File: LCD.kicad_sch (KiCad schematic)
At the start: 1 part, among them U5 LCD_ILI9341

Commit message: sebelum pemeriksaan terkahir
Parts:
- added BZ1: Buzzer, symbol Device:Buzzer
- added C73: 4.7uF, symbol Device:C
- added R47: 100 ohm, symbol Device:R_US
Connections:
- net GND: now also BZ1.2 (-), C73.2
- net ILI9341_VCC renamed DCDC_3V3
- net DCDC_3V3: now also C73.1
- new net: BZ1.1 (+), R47.2
- new net buzzer: R47.1

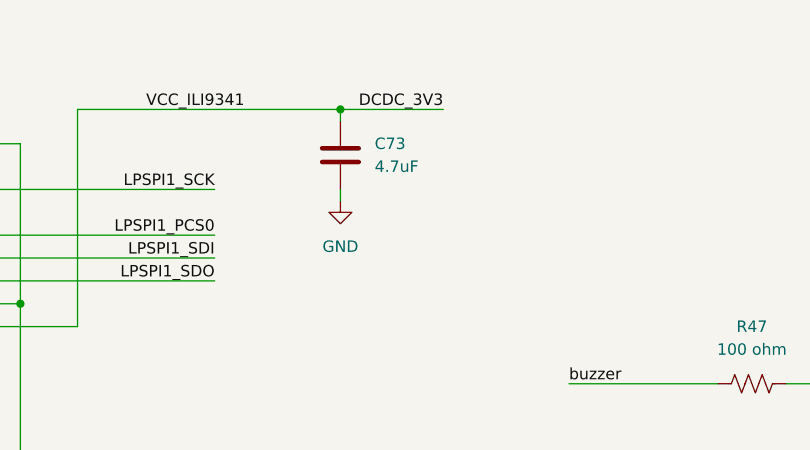
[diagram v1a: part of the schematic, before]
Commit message: menambah lebih dari setengah footprint
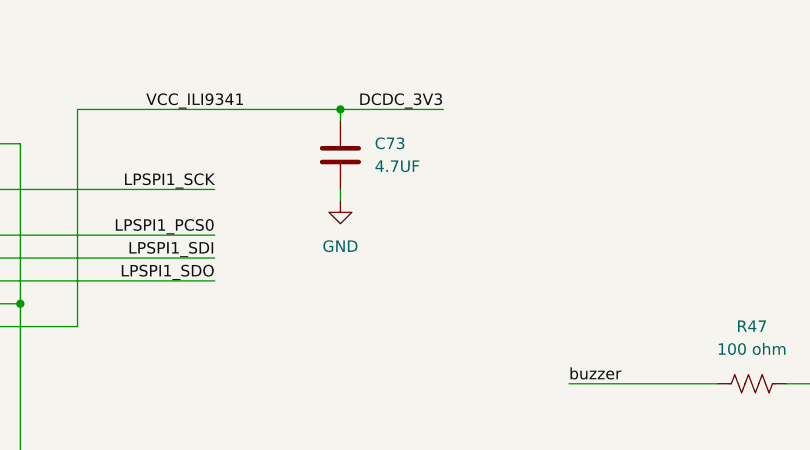
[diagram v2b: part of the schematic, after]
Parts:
- C73: value 4.7uF -> 4.7UF; footprint (none) -> Capacitor_SMD:C_0402_1005Metric; MANUFACTURER (none) -> C1005X5R0J475M050BC
- R47: footprint (none) -> Resistor_SMD:R_0402_1005Metric
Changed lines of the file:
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@@
+			)
+		)
+		(property "DigikeyPartNumber" ""
+			(at 196.85 62.23 0)
+			(effects
+				(font
+					(size 1.27 1.27)
+				)
+				(hide yes)
 			)
 		)
@@
 			)
 		)
-		(property "Value" "4.7uF"
+		(property "Value" "4.7UF"
 			(at 142.24 35.5599 0)
 			(effects
@@
 			)
 		)
-		(property "Footprint" ""
+		(property "Footprint" "Capacitor_SMD:C_0402_1005Metric"
 			(at 139.3952 38.1 0)
 			(effects
@@
 			)
 		)
+		(property "DigikeyPartNumber" ""
+			(at 138.43 34.29 0)
+			(effects
+				(font
+					(size 1.27 1.27)
+				)
+				(hide yes)
+			)
+		)
+		(property "MANUFACTURER" "C1005X5R0J475M050BC "
+			(at 138.43 34.29 0)
+			(effects
+				(font
+					(size 1.27 1.27)
+				)
+				(hide yes)
+			)
+		)
 		(pin "1"
 		)
@@
 			)
 		)
-		(property "Footprint" ""
+		(property "Footprint" "Resistor_SMD:R_0402_1005Metric"
 			(at 184.404 58.674 90)
 			(effects
@@
 			)
 		)
+		(property "DigikeyPartNumber" ""
+			(at 184.15 59.69 0)
+			(effects
+				(font
+					(size 1.27 1.27)
+				)
+				(hide yes)
+			)
+		)
 		(pin "2"
 		)
@@
 			(effects
 				(font
+					(size 1.27 1.27)
+				)
+				(hide yes)
+			)
+		)
+		(property "DigikeyPartNumber" ""
+			(at 39.37 54.61 0)
+			(effects
+				(font
